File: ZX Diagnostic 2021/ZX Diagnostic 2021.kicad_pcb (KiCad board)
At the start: 2 copper layers, 57.9 x 61.6 mm, 31 parts, among them J1 Cartridge, M1 Mounting, M2 Mounting, M3 Mounting, M4 Mounting, U1 27C512, U2 74HCT373

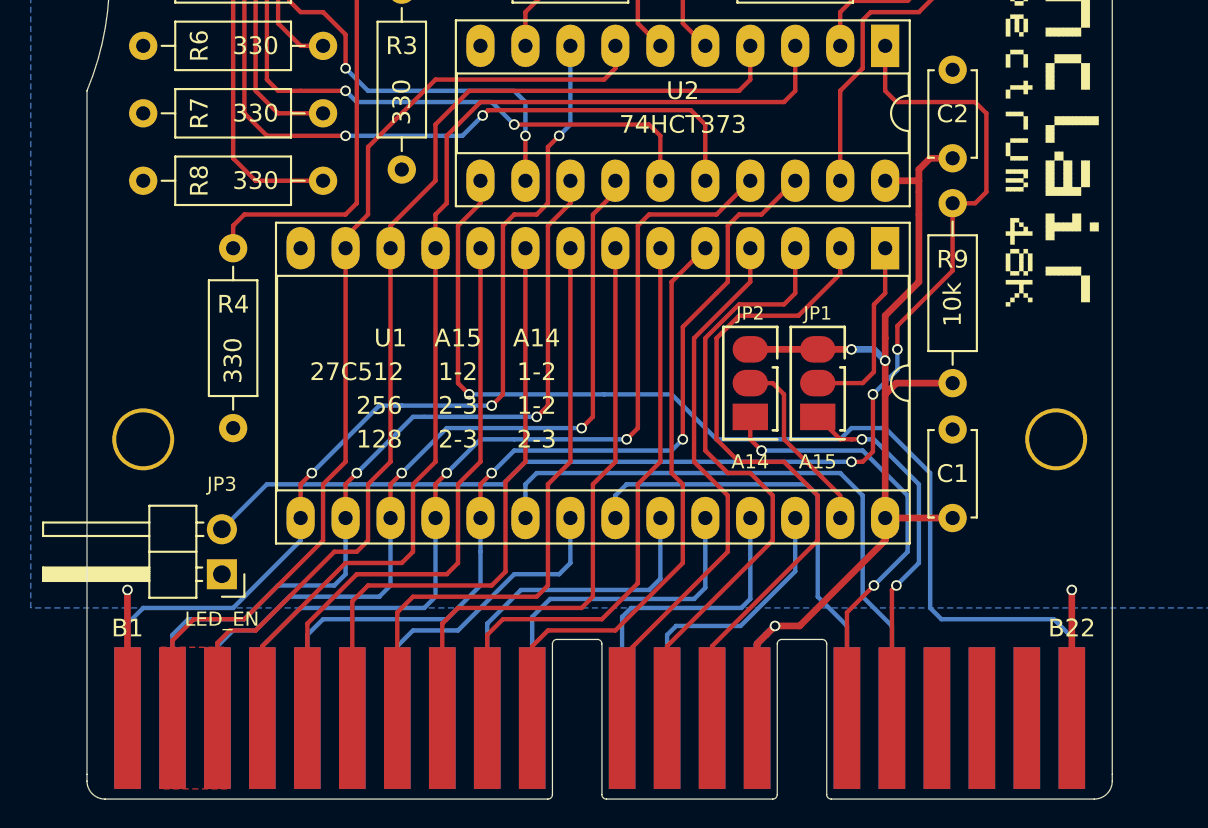
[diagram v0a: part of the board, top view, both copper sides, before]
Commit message: Fixed diagnostic pinout
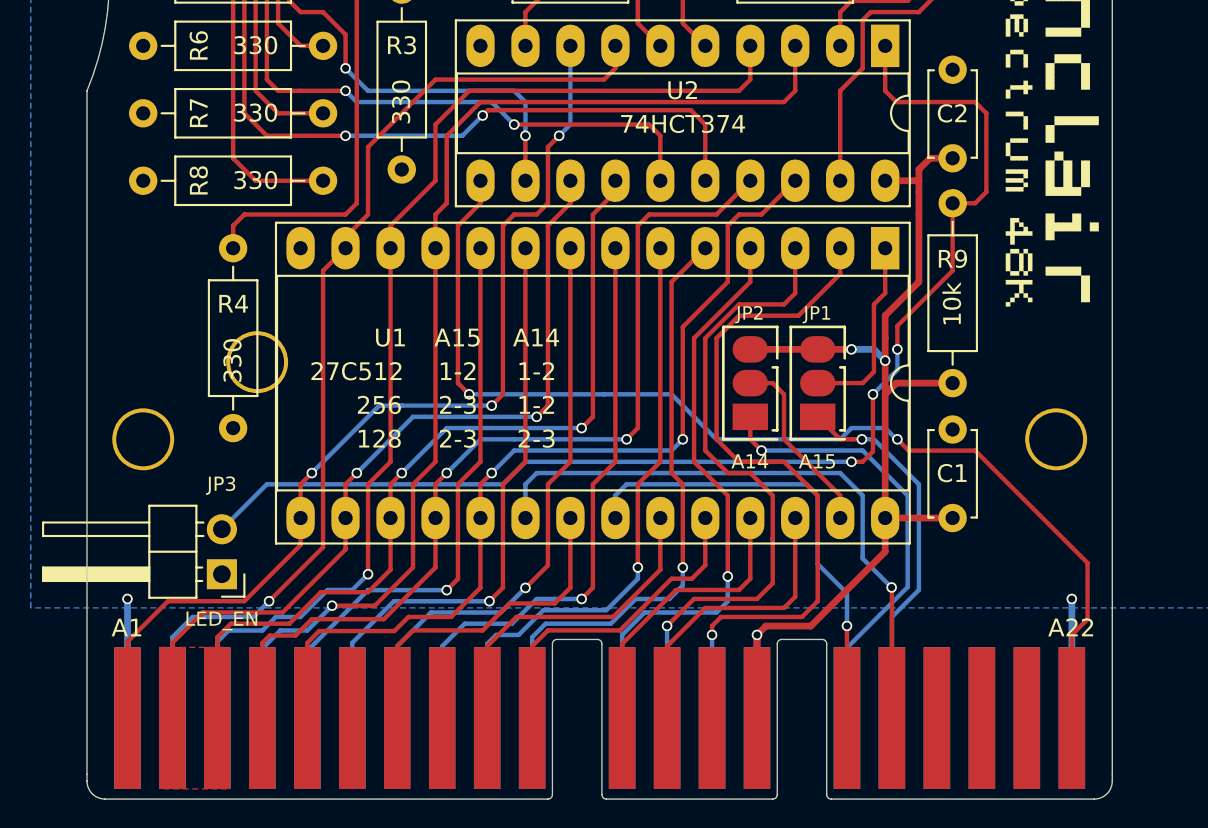
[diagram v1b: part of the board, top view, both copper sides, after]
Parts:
- removed the sinclair_title at (177.5, 93.3)
- added M1: Mounting, mounting:M3_pin, F.Cu at (129.9, 96.0)
- U2: value 74HCT373 -> 74HCT374
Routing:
- net /A12: track 37.7 -> 40.4 mm, vias 0 -> 1
- net /A6: track 31.1 -> 33.5 mm, vias 0 -> 1
- net /A7: track 34.9 -> 37.1 mm, vias 0 -> 1
- net /A9: track 20.5 -> 18.4 mm
- net /A2: track 34.7 -> 32.9 mm, vias 0 -> 1
- net /A8: track 17.9 -> 16.4 mm
- net /D1: track 61.0 -> 62.1 mm, vias 0 -> 1
- net /D4: track 47.5 -> 46.4 mm
- net /A5: track 33.4 -> 34.4 mm, vias 0 -> 1
- net /A11: track 19.6 -> 18.6 mm
- net /A3: track 34.7 -> 33.6 mm, vias 0 -> 1
- net GND: track 14.5 -> 13.5 mm
- net /A1: track 34.7 -> 33.8 mm, vias 0 -> 1
- net /D6: track 52.9 -> 52.1 mm
- net /A10: track 18.3 -> 19.1 mm
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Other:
- board text added: "LED_EN"

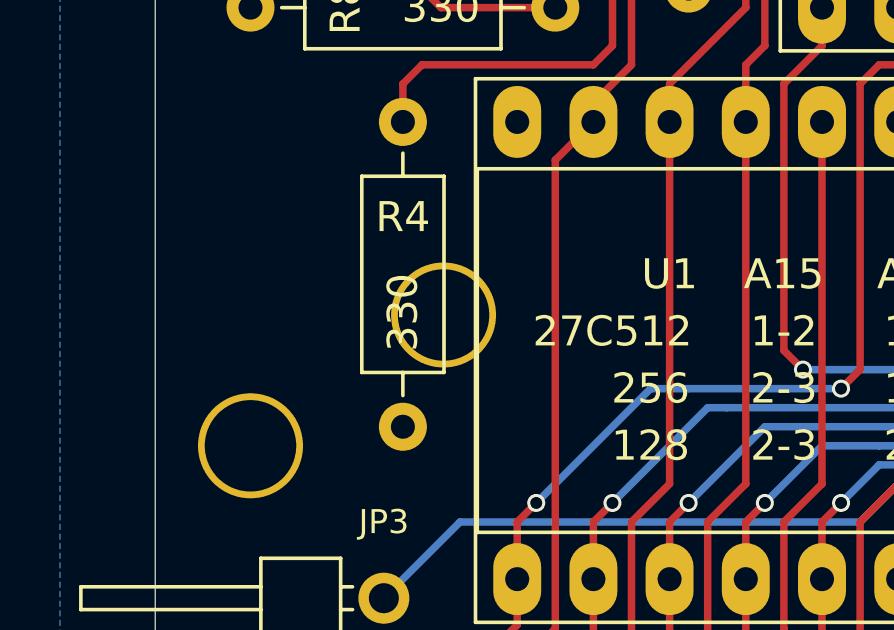
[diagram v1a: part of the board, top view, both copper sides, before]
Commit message: Fixed a mounting pin bug
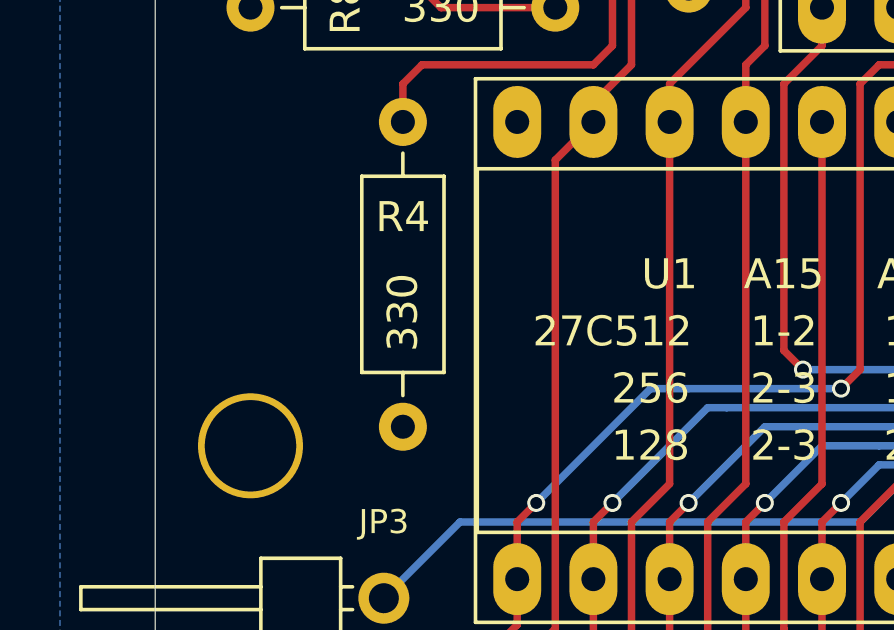
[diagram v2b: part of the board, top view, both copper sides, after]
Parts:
- removed the M1 at (129.9, 96.0)
